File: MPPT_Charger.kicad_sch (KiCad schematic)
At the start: 114 parts, among them J1 Solar, J2 Battery, J3 USB_B_Mini, J4 INTERFACE PORT, J6 JTAG, J8 Micro_SD_Card_Det_Hirose_DM3AT, J9 IIC RTC, Q1 CSD19505KCS, Q11 CSD19505KCS, Q12 CSD19505KCS, Q13 CSD19505KCS, Q2 CSD19505KCS, Q3 CSD19505KCS, Q4 Si2306, Q5 MMBT3904 1A, Q6 MMBT3904 1A, Q7 Si2306, U1 ACS712, U10 ADS1015, U2 B1212S, U3 AMS1117-5.0, U4 AMS1117-3.3, U5 XL7005A, U6 XL7005A, U7 IR2104, U8 ESP32, U9 CH340G

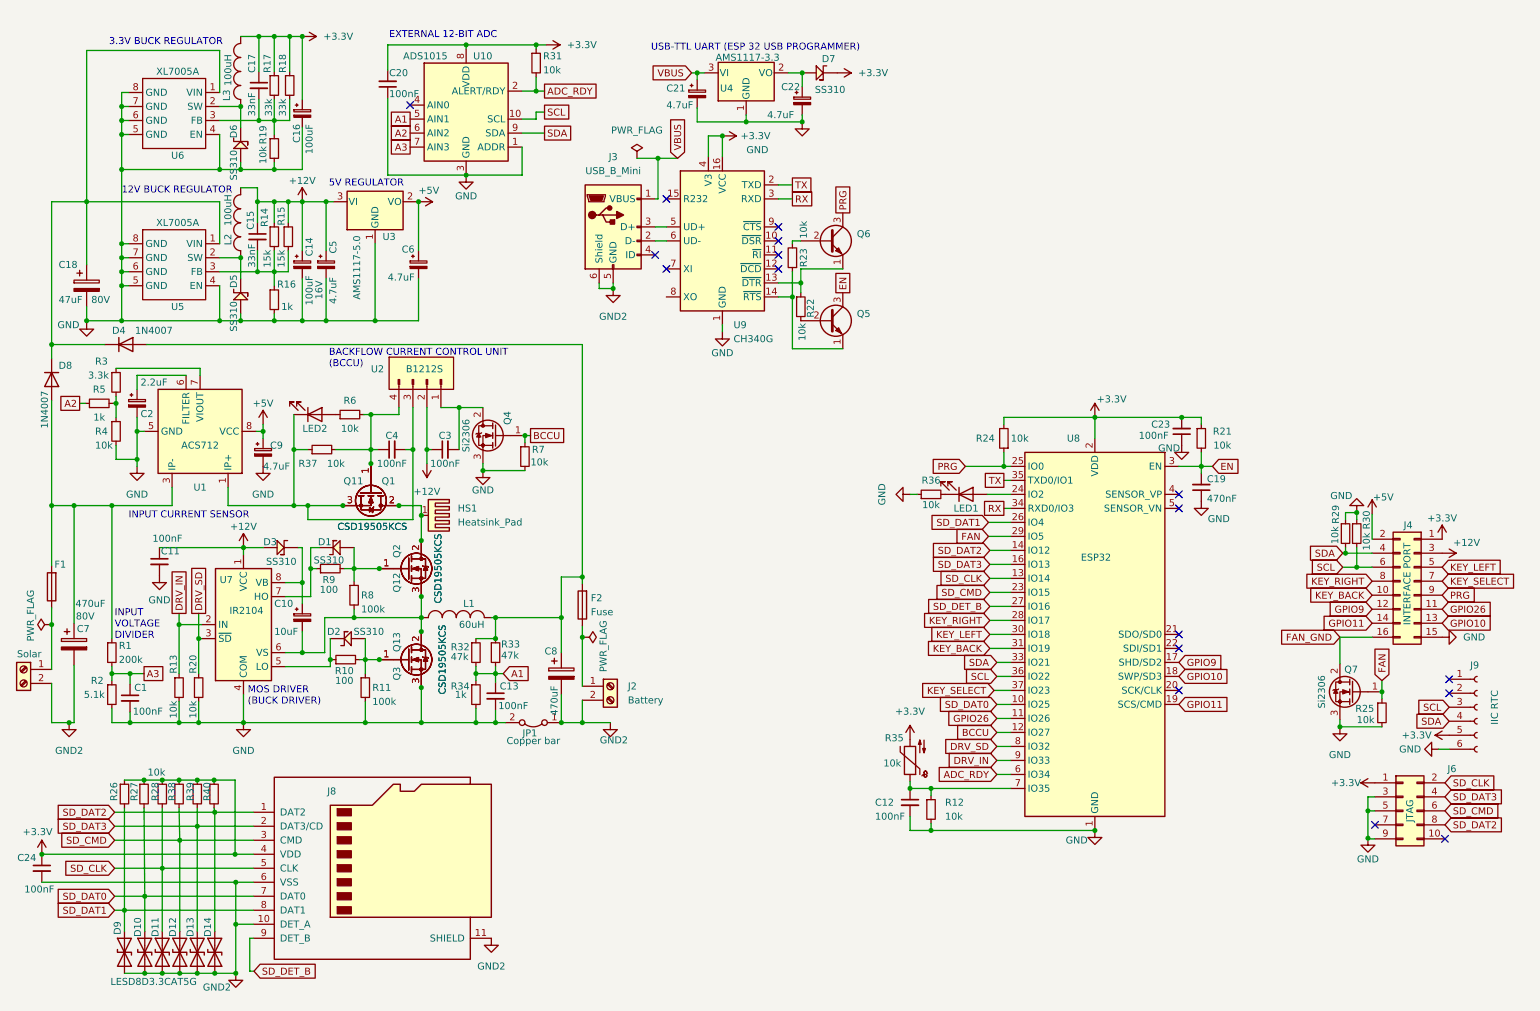
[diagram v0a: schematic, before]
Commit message: Reworked layout. Changed a few pins. Double power transistors removed. Traces would not be able to support the amperage anyway.
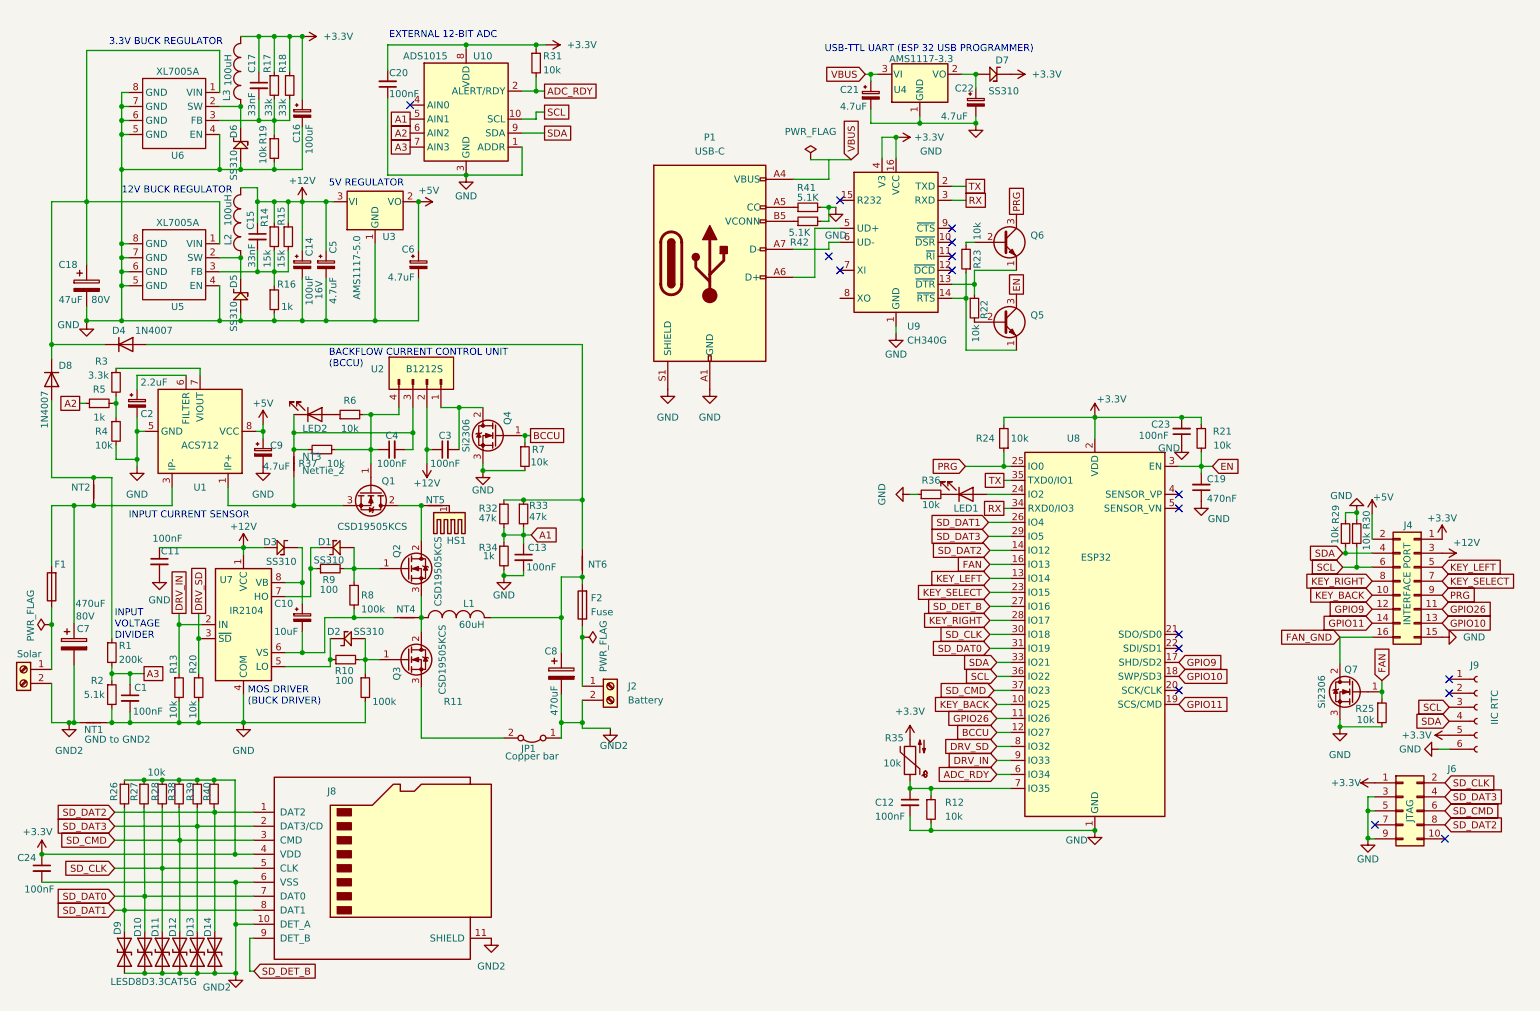
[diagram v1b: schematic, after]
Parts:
- removed J3: USB_B_Mini, Connector_USB:USB_Mini-B_Lumberg_2486_01_Horizontal, symbol Connector:USB_B_Mini
- removed Q11, Q12: CSD19505KCS, Package_TO_SOT_THT:TO-220-3_Vertical, symbol footprint:CSD19505KCS
- removed Q13: CSD19505KCS, Library:TO-220-3_Vertical_Insulated, symbol footprint:CSD19505KCS
- added NT1: GND to GND2, NetTie:NetTie-2_SMD_Pad0.5mm, symbol Device:NetTie_2
- added NT2, NT3, NT4, NT5, NT6: NetTie_2, NetTie:NetTie-2_SMD_Pad0.5mm, symbol Device:NetTie_2
- added P1: USB-C, Connector_USB:USB_C_Receptacle_GCT_USB4105-xx-A_16P_TopMnt_Horizontal, symbol Connector:USB_C_Plug_USB2.0
- added R41, R42: 5.1K, Resistor_SMD:R_0603_1608Metric, symbol Device:R_Small
- F1, F2: footprint Fuse:Fuse_Blade_ATO_directSolder -> Library:Fuse_Blade_ATO_directSolder
- J8: footprint AA:microSD_HC_Molex_104031-0811 -> Library:microSD_HC_Molex_104031-0811
- Q3: footprint Library:TO-220-3_Vertical_Insulated -> Library:Package_TO_SOT_THTTO-220-3_Vertical_Insulated
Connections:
- net FAN: now also U8.16 (IO13); no longer U8.29 (IO5)
- net GND: now also NT1.1, P1.A1 (GND), P1.A12 (GND), P1.B1 (GND), P1.B12 (GND), P1.S1 (SHIELD), R41.2, R42.2; no longer JP1.2 (B), Q3.3 (S)
- net GND2: now also NT1.2
- net KEY_BACK: now also U8.10 (IO25); no longer U8.31 (IO19)
- net KEY_LEFT: now also U8.13 (IO14); no longer U8.30 (IO18)
- net KEY_SELECT: now also U8.23 (IO15); no longer U8.37 (IO23)
- net SD_CLK: now also U8.30 (IO18); no longer U8.13 (IO14)
- net SD_CMD: now also U8.37 (IO23); no longer U8.23 (IO15)
- net SD_DAT0: now also U8.31 (IO19); no longer U8.10 (IO25)
- net SD_DAT3: now also U8.29 (IO5); no longer U8.16 (IO13)
- net at C8.1, F2.2, L1.2: now also NT6.1; no longer D4.2 (A), R32.1, R33.1
- net at Q1.2 (D), Q2.2 (D): now also NT5.2; no longer HS1.1
- net at C4.2, LED2.1 (K), R37.1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: now also NT3.2; no longer Q1.3 (S), U1.1 (IP+), U1.2 (IP+)
- net at C7.1, F1.2, U1.3 (IP-)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: now also NT2.2; no longer D8.2 (A), R1.1
- net at C10.2, R8.2, U7.6 (VS): now also NT4.1; no longer L1.1, Q2.3 (S), Q3.2 (D)
- net at U9.6 (UD-): now also P1.A7 (D-)
- net at U9.5 (UD+): now also P1.A6 (D+)
- new net: HS1.1, NT5.1
- new net: L1.1, NT4.2, Q2.3 (S), Q3.2 (D)
- new net: JP1.2 (B), Q3.3 (S)
- new net: P1.B5 (VCONN), R42.1
- new net: D8.2 (A), NT2.1, R1.1
- new net: D4.2 (A), NT6.2, R32.1, R33.1
- new net: NT3.1, Q1.3 (S), U1.1 (IP+), U1.2 (IP+)
- new net: P1.A5 (CC), R41.1
- new net: P1.A4 (VBUS), P1.A9 (VBUS), P1.B4 (VBUS), P1.B9 (VBUS)
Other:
- moved on the sheet: C13, C21, C22, D7, HS1, JP1, Q5, Q6, R22, R23, R32, R33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

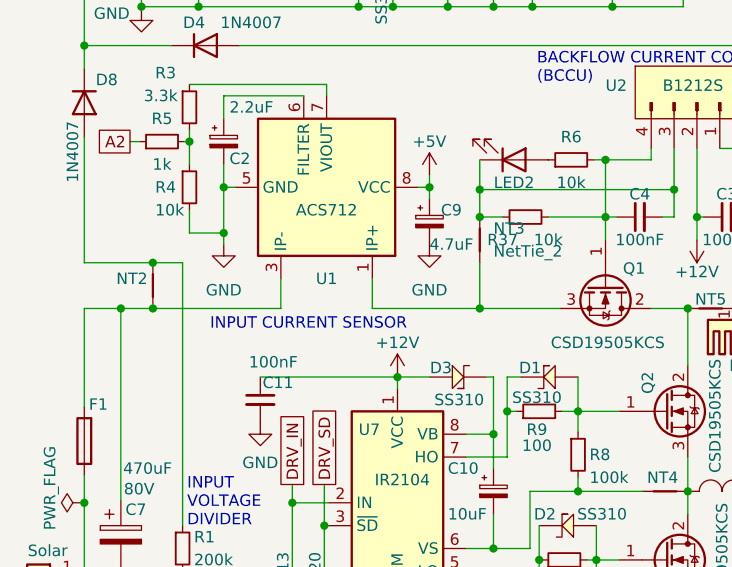
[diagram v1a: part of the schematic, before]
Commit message: Some manual corrections, and some too small footprints updated.
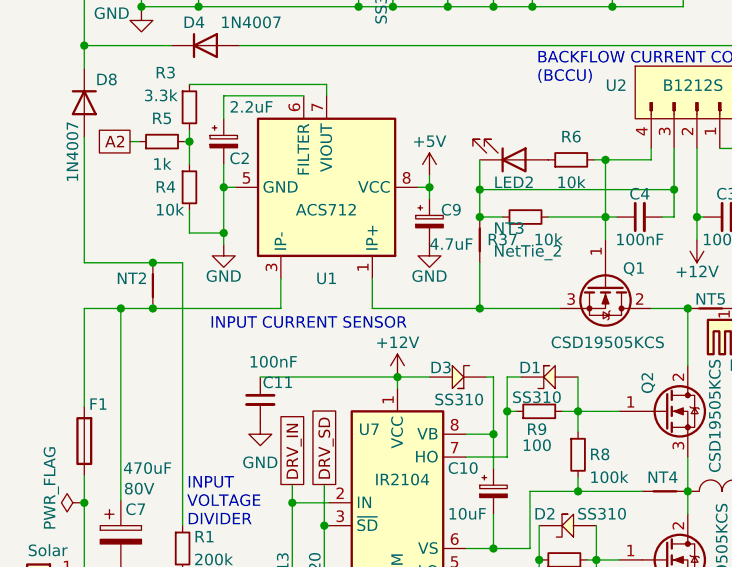
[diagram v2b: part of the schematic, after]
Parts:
- C10: footprint Capacitor_SMD:C_Elec_5x5.4 -> Capacitor_Tantalum_SMD:CP_EIA-3216-10_Kemet-I
- C18: footprint Capacitor_SMD:C_Elec_6.3x5.8 -> Capacitor_SMD:CP_Elec_10x10.5
- C21, C22, C6, C9: footprint Capacitor_SMD:C_0603_1608Metric -> Capacitor_SMD:C_0805_2012Metric
- D1, D2, D3, D4, D5, D6, D7, D8: footprint AA:DO-214AA -> Diode_SMD:D_SMB
- P1: footprint Connector_USB:USB_C_Receptacle_GCT_USB4105-xx-A_16P_TopMnt_Horizontal -> Connector_USB:USB_C_Receptacle_GCT_USB4125-xx-x_6P_TopMnt_Horizontal
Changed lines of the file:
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@@
 			)
 		)
-		(property "Footprint" "AA:DO-214AA"
+		(property "Footprint" "Diode_SMD:D_SMB"
 			(at 196.85 12.7 0)
 			(effects
@@
 		(on_board yes)
 		(dnp no)
-		(fields_autoplaced yes)
 		(property "Reference" "#PWR0104"
 			(at 58.674 99.06 0)
@@
 		)
 		(property "Value" "GND"
-			(at 58.674 97.79 0)
+			(at 58.674 96.266 0)
 			(effects
 				(font
@@
 			)
 		)
-		(property "Footprint" "AA:DO-214AA"
+		(property "Footprint" "Diode_SMD:D_SMB"
 			(at 45.72 56.134 0)
 			(effects
@@
 			)
 		)
-		(property "Footprint" "Capacitor_SMD:C_Elec_5x5.4"
+		(property "Footprint" "Capacitor_Tantalum_SMD:CP_EIA-3216-10_Kemet-I"
 			(at 65.786 120.142 0)
 			(effects
@@
 			)
 		)
-		(property "Footprint" "AA:DO-214AA"
+		(property "Footprint" "Diode_SMD:D_SMB"
 			(at 45.72 28.702 0)
 			(effects
@@
 			)
 		)
-		(property "Footprint" "Capacitor_SMD:C_0603_1608Metric"
+		(property "Footprint" "Capacitor_SMD:C_0805_2012Metric"
 			(at 86.868 56.134 0)
 			(effects
@@
 			)
 		)
-		(property "Footprint" "Capacitor_SMD:C_Elec_6.3x5.8"
+		(property "Footprint" "Capacitor_SMD:CP_Elec_10x10.5"
 			(at 27.6352 63.754 0)
 			(effects
@@
 			)
 		)
-		(property "Footprint" "Capacitor_SMD:C_0603_1608Metric"
+		(property "Footprint" "Capacitor_SMD:C_0805_2012Metric"
 			(at 168.91 25.4 0)
 			(effects
@@
 			)
 		)
-		(property "Footprint" "AA:DO-214AA"
+		(property "Footprint" "Diode_SMD:D_SMB"
 			(at 68.326 132.842 0)
 			(effects
@@
 			)
 		)
-		(property "Footprint" "AA:DO-214AA"
+		(property "Footprint" "Diode_SMD:D_SMB"
 			(at 15.875 76.962 0)
 			(effects
@@
 			)
 		)
-		(property "Footprint" "Capacitor_SMD:C_0603_1608Metric"
+		(property "Footprint" "Capacitor_SMD:C_0805_2012Metric"
 			(at 187.96 26.67 0)
 			(effects
@@
 		(on_board yes)
 		(dnp no)
-		(fields_autoplaced yes)
 		(property "Reference" "#PWR0103"
 			(at 35.814 99.06 0)
@@
 		)
 		(property "Value" "GND"
-			(at 35.814 97.79 0)
+			(at 35.814 96.266 0)
 			(effects
 				(font
@@
 			)
 		)
-		(property "Footprint" "AA:DO-214AA"
+		(property "Footprint" "Diode_SMD:D_SMB"
 			(at 33.782 75.057 0)
 			(effects
@@
 			)
 		)
-		(property "Footprint" "AA:DO-214AA"
+		(property "Footprint" "Diode_SMD:D_SMB"
 			(at 66.294 116.332 0)
 			(effects
@@
 			)
 		)
-		(property "Footprint" "Capacitor_SMD:C_0603_1608Metric"
+		(property "Footprint" "Capacitor_SMD:C_0805_2012Metric"
 			(at 58.674 90.17 0)
 			(effects
@@
 			)
 		)
-		(property "Footprint" "Connector_USB:USB_C_Receptacle_GCT_USB4105-xx-A_16P_TopMnt_Horizontal"
+		(property "Footprint" "Connector_USB:USB_C_Receptacle_GCT_USB4125-xx-x_6P_TopMnt_Horizontal"
 			(at 143.51 55.88 0)
 			(effects
@@
 			)
 		)
-		(property "Footprint" "AA:DO-214AA"
+		(property "Footprint" "Diode_SMD:D_SMB"
 			(at 67.564 98.552 0)
 			(effects
